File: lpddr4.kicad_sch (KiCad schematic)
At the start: 1 part, among them U2 MT53E1G32D2FW-046 IT:B

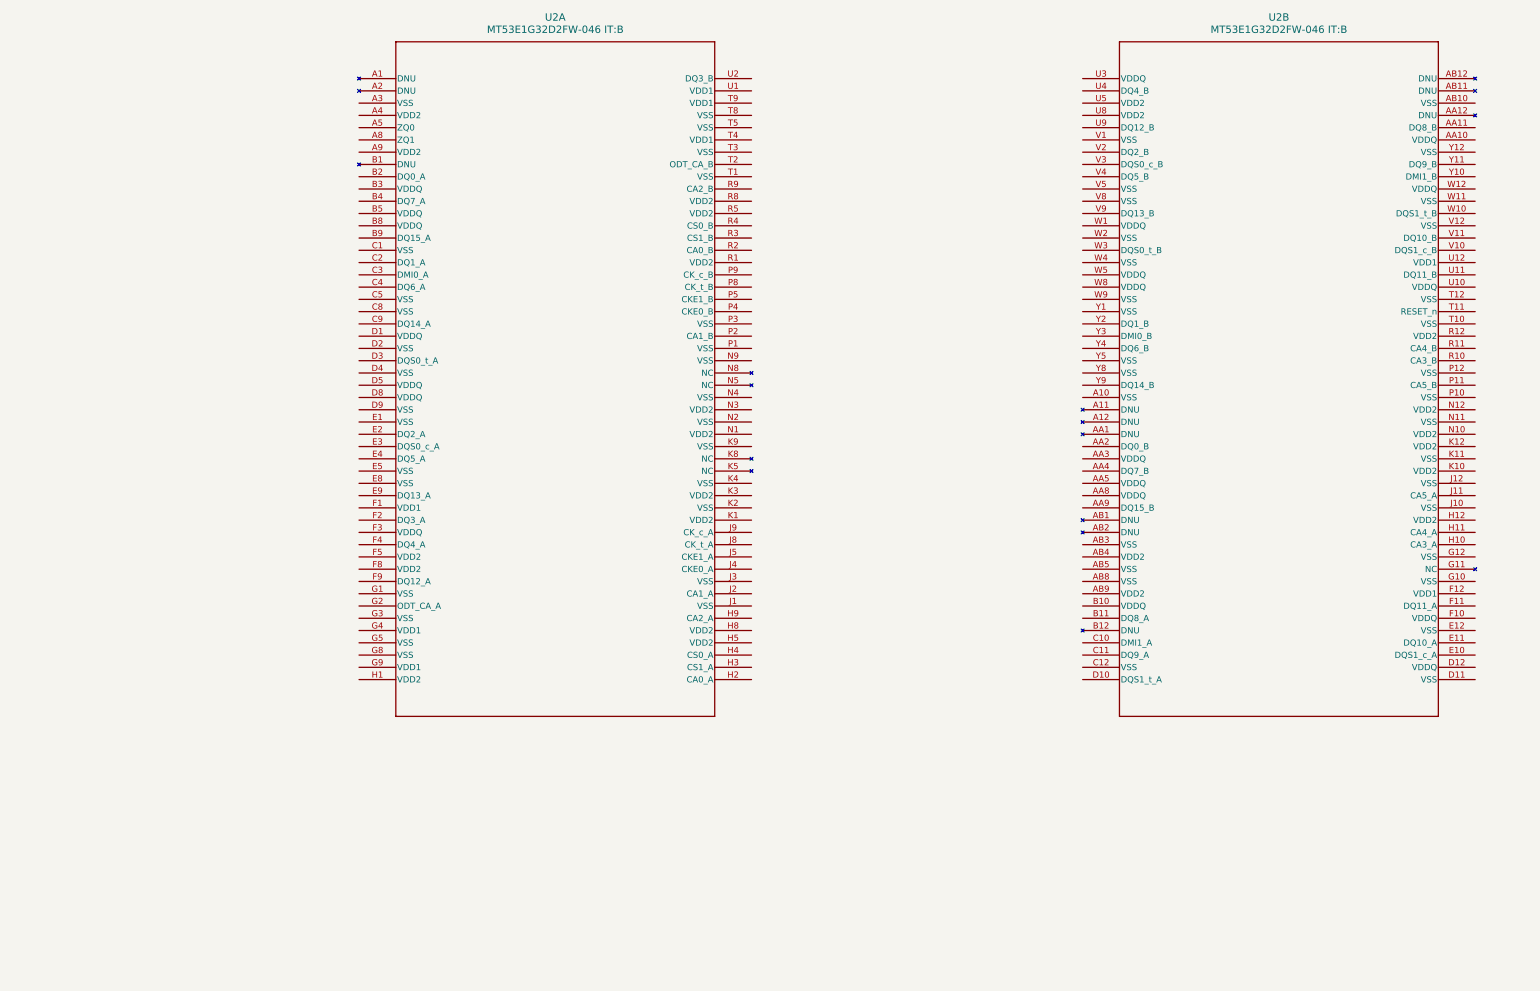
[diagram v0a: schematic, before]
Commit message: connected lpddr4 to mp
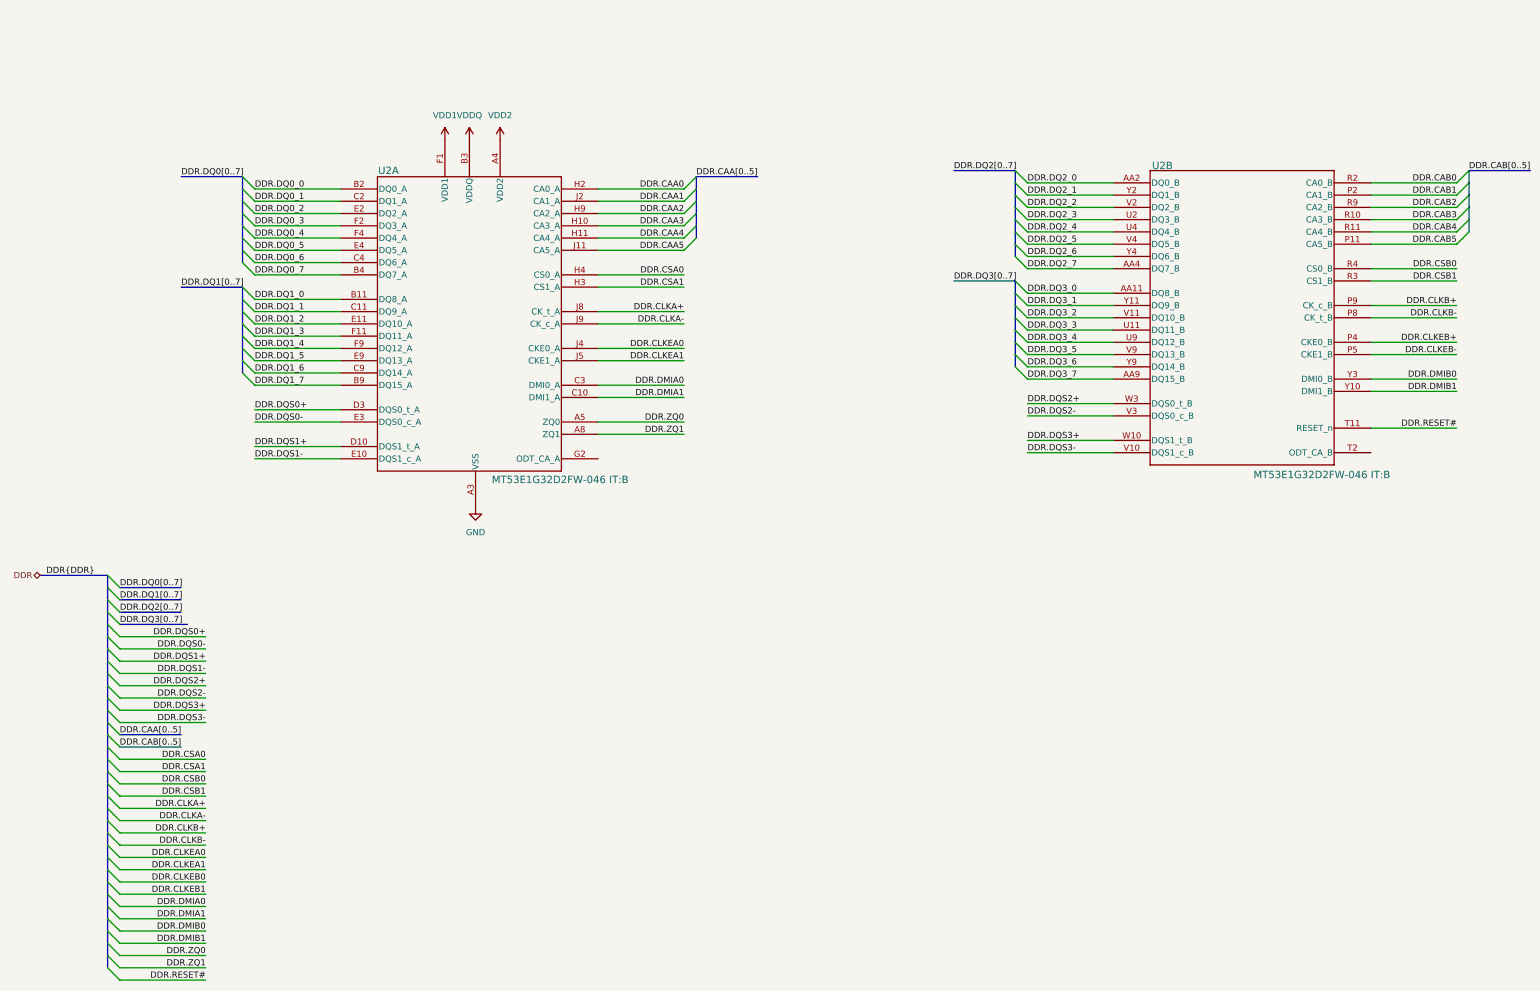
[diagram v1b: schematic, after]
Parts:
- U2: footprint VFBGA200_10X14.5X1.1FW_MRN -> MT53E1G32D2FW-046-IT-B:VFBGA200_10X14.5X1.1FW_MRN-L
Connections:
- net at U2.A1 (DNU): now also U2.A11 (DNU), U2.A12 (DNU), U2.A2 (DNU), U2.AA1 (DNU), U2.AA12 (DNU), U2.AB1 (DNU), U2.AB11 (DNU), U2.AB12 (DNU), U2.AB2 (DNU), U2.B1 (DNU), U2.B12 (DNU)
- net GND: now reaches U2.A3 (VSS)
- net GND: now also U2.A10 (VSS), U2.AB10 (VSS), U2.AB3 (VSS), U2.AB5 (VSS), U2.AB8 (VSS), U2.C1 (VSS), U2.C12 (VSS), U2.C5 (VSS), U2.C8 (VSS), U2.D11 (VSS), U2.D2 (VSS), U2.D4 (VSS), U2.D9 (VSS), U2.E1 (VSS), U2.E12 (VSS), U2.E5 (VSS), U2.E8 (VSS), U2.G1 (VSS), U2.G10 (VSS), U2.G12 (VSS), U2.G3 (VSS), U2.G5 (VSS), U2.G8 (VSS), U2.J1 (VSS), U2.J10 (VSS), U2.J12 (VSS), U2.J3 (VSS), U2.K11 (VSS), U2.K2 (VSS), U2.K4 (VSS), U2.K9 (VSS), U2.N11 (VSS), U2.N2 (VSS), U2.N4 (VSS), U2.N9 (VSS), U2.P1 (VSS), U2.P10 (VSS), U2.P12 (VSS), U2.P3 (VSS), U2.T1 (VSS), U2.T10 (VSS), U2.T12 (VSS), U2.T3 (VSS), U2.T5 (VSS), U2.T8 (VSS), U2.V1 (VSS), U2.V12 (VSS), U2.V5 (VSS), U2.V8 (VSS), U2.W11 (VSS), U2.W2 (VSS), U2.W4 (VSS), U2.W9 (VSS), U2.Y1 (VSS), U2.Y12 (VSS), U2.Y5 (VSS), U2.Y8 (VSS)
- net VDD2: now reaches U2.A4 (VDD2)
- net VDD2: now also U2.A9 (VDD2), U2.AB4 (VDD2), U2.AB9 (VDD2), U2.F5 (VDD2), U2.F8 (VDD2), U2.H1 (VDD2), U2.H12 (VDD2), U2.H5 (VDD2), U2.H8 (VDD2), U2.K1 (VDD2), U2.K10 (VDD2), U2.K12 (VDD2), U2.K3 (VDD2), U2.N1 (VDD2), U2.N10 (VDD2), U2.N12 (VDD2), U2.N3 (VDD2), U2.R1 (VDD2), U2.R12 (VDD2), U2.R5 (VDD2), U2.R8 (VDD2), U2.U5 (VDD2), U2.U8 (VDD2)
- net DDR.ZQ0: now reaches U2.A5 (ZQ0)
- net DDR.ZQ1: now reaches U2.A8 (ZQ1)
- net DDR.DQ0_0: now reaches U2.B2 (DQ0_A)
- net VDDQ: now reaches U2.B3 (VDDQ)
- net VDDQ: now also U2.AA10 (VDDQ), U2.AA3 (VDDQ), U2.AA5 (VDDQ), U2.AA8 (VDDQ), U2.B10 (VDDQ), U2.B5 (VDDQ), U2.B8 (VDDQ), U2.D1 (VDDQ), U2.D12 (VDDQ), U2.D5 (VDDQ), U2.D8 (VDDQ), U2.F10 (VDDQ), U2.F3 (VDDQ), U2.U10 (VDDQ), U2.U3 (VDDQ), U2.W1 (VDDQ), U2.W12 (VDDQ), U2.W5 (VDDQ), U2.W8 (VDDQ)
- net DDR.DQ0_7: now reaches U2.B4 (DQ7_A)
- net DDR.DQ1_7: now reaches U2.B9 (DQ15_A)
- net DDR.DQ0_1: now reaches U2.C2 (DQ1_A)
- net DDR.DMIA0: now reaches U2.C3 (DMI0_A)
- net DDR.DQ0_6: now reaches U2.C4 (DQ6_A)
- net DDR.DQ1_6: now reaches U2.C9 (DQ14_A)
- net DDR.DQS0+: now reaches U2.D3 (DQS0_t_A)
- net DDR.DQ0_2: now reaches U2.E2 (DQ2_A)
- net DDR.DQS0-: now reaches U2.E3 (DQS0_c_A)
- net DDR.DQ0_5: now reaches U2.E4 (DQ5_A)
- net DDR.DQ1_5: now reaches U2.E9 (DQ13_A)
- net VDD1: now reaches U2.F1 (VDD1)
- net VDD1: now also U2.F12 (VDD1), U2.G4 (VDD1), U2.G9 (VDD1), U2.T4 (VDD1), U2.T9 (VDD1), U2.U1 (VDD1), U2.U12 (VDD1)
- net DDR.DQ0_3: now reaches U2.F2 (DQ3_A)
- net DDR.DQ0_4: now reaches U2.F4 (DQ4_A)
- net DDR.DQ1_4: now reaches U2.F9 (DQ12_A)
- net DDR.CAA0: now reaches U2.H2 (CA0_A)
- net DDR.CSA1: now reaches U2.H3 (CS1_A)
- net DDR.CSA0: now reaches U2.H4 (CS0_A)
- net DDR.CAA2: now reaches U2.H9 (CA2_A)
- net DDR.CAA1: now reaches U2.J2 (CA1_A)
- net DDR.CLKEA0: now reaches U2.J4 (CKE0_A)
- net DDR.CLKEA1: now reaches U2.J5 (CKE1_A)
- net DDR.CLKA+: now reaches U2.J8 (CK_t_A)
- net DDR.CLKA-: now reaches U2.J9 (CK_c_A)
- net at U2.K5 (NC): now also U2.G11 (NC), U2.K8 (NC), U2.N5 (NC), U2.N8 (NC)
- net DDR.DQ3_0: now reaches U2.AA11 (DQ8_B)
- net DDR.DQ2_0: now reaches U2.AA2 (DQ0_B)
- net DDR.DQ2_7: now reaches U2.AA4 (DQ7_B)
- net DDR.DQ3_7: now reaches U2.AA9 (DQ15_B)
- net DDR.CAB5: now reaches U2.P11 (CA5_B)
- net DDR.CAB3: now reaches U2.R10 (CA3_B)
- net DDR.CAB4: now reaches U2.R11 (CA4_B)
- net DDR.RESET#: now reaches U2.T11 (RESET_n)
- net DDR.DQ3_3: now reaches U2.U11 (DQ11_B)
- net DDR.DQ2_4: now reaches U2.U4 (DQ4_B)
- net DDR.DQ3_4: now reaches U2.U9 (DQ12_B)
- net DDR.DQS3-: now reaches U2.V10 (DQS1_c_B)
- net DDR.DQ3_2: now reaches U2.V11 (DQ10_B)
- net DDR.DQ2_2: now reaches U2.V2 (DQ2_B)
- net DDR.DQS2-: now reaches U2.V3 (DQS0_c_B)
- net DDR.DQ2_5: now reaches U2.V4 (DQ5_B)
- net DDR.DQ3_5: now reaches U2.V9 (DQ13_B)
- net DDR.DQS3+: now reaches U2.W10 (DQS1_t_B)
- net DDR.DQS2+: now reaches U2.W3 (DQS0_t_B)
- net DDR.DMIB1: now reaches U2.Y10 (DMI1_B)
- net DDR.DQ3_1: now reaches U2.Y11 (DQ9_B)
- net DDR.DQ2_1: now reaches U2.Y2 (DQ1_B)
- net DDR.DMIB0: now reaches U2.Y3 (DMI0_B)
- net DDR.DQ2_6: now reaches U2.Y4 (DQ6_B)
- net DDR.DQ3_6: now reaches U2.Y9 (DQ14_B)
- new net DDR.CAA3: U2.H10 (CA3_A)
- new net DDR.CAA4: U2.H11 (CA4_A)
- new net DDR.CAA5: U2.J11 (CA5_A)
- new net DDR.CAB0: U2.R2 (CA0_B)
- new net DDR.CAB1: U2.P2 (CA1_B)
- new net DDR.CAB2: U2.R9 (CA2_B)
- new net DDR.CLKB+: U2.P9 (CK_c_B)
- new net DDR.CLKB-: U2.P8 (CK_t_B)
- new net DDR.CLKEB+: U2.P4 (CKE0_B)
- new net DDR.CLKEB-: U2.P5 (CKE1_B)
- new net DDR.CSB0: U2.R4 (CS0_B)
- new net DDR.CSB1: U2.R3 (CS1_B)
- new net DDR.DMIA1: U2.C10 (DMI1_A)
- new net DDR.DQ1_0: U2.B11 (DQ8_A)
- new net DDR.DQ1_1: U2.C11 (DQ9_A)
- new net DDR.DQ1_2: U2.E11 (DQ10_A)
- new net DDR.DQ1_3: U2.F11 (DQ11_A)
- new net DDR.DQ2_3: U2.U2 (DQ3_B)
- new net DDR.DQS1+: U2.D10 (DQS1_t_A)
- new net DDR.DQS1-: U2.E10 (DQS1_c_A)

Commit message: got started on the pmic
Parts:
- added R1: 10k, symbol Device:R
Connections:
- net DDR.RESET#: now also R1.1
- net GND: now also R1.2
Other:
- note added: "TODO: package is wrong :("
